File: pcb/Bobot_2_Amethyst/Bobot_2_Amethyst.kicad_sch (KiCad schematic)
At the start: 2 parts

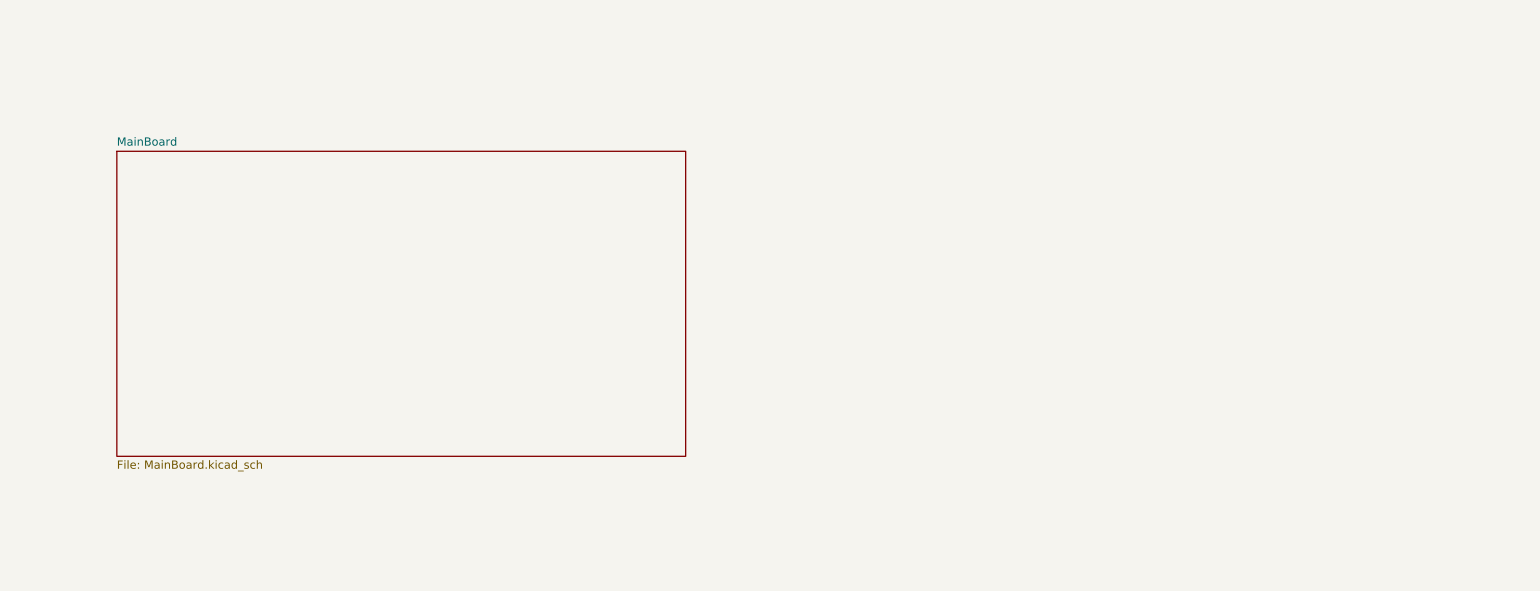
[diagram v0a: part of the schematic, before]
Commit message: pcb: add touch sensor board
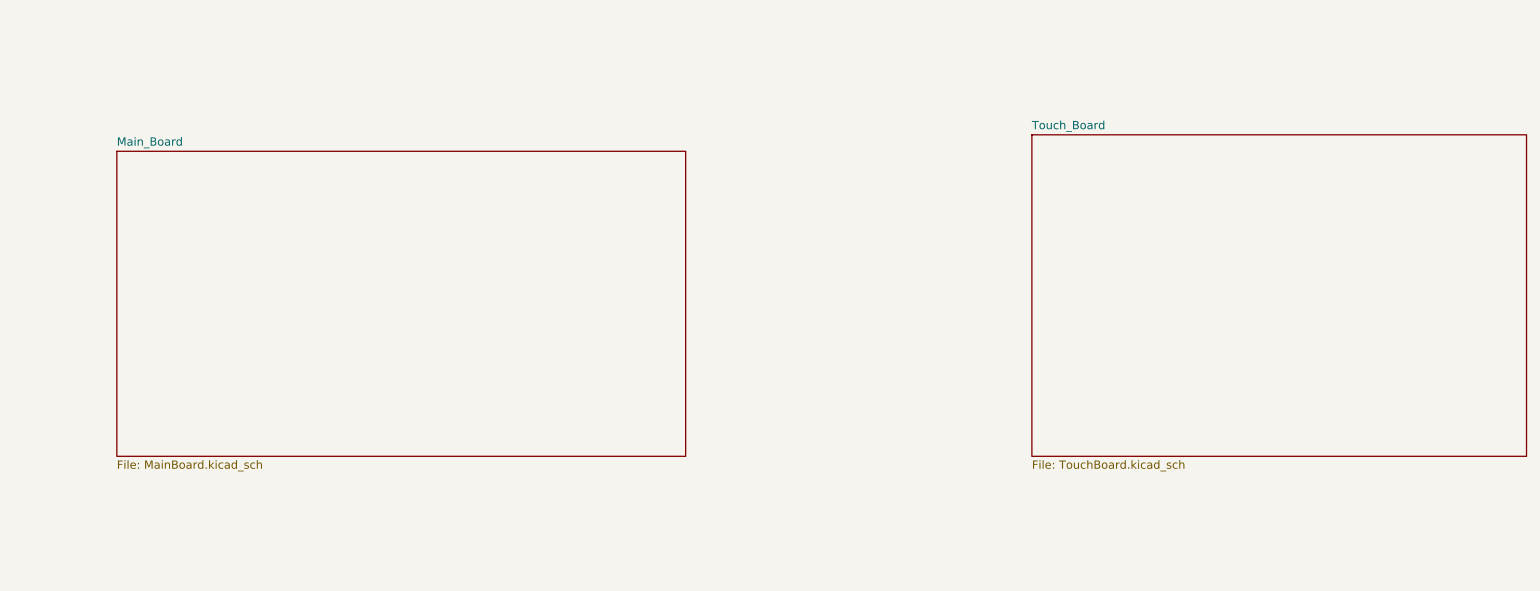
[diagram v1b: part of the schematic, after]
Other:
- sheet MainBoard renamed Main_Board
- added sheet Touch_Board (TouchBoard.kicad_sch)
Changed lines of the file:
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@@
 			(color 0 0 0 0.0000)
 		)
-		(property "Sheetname" "MainBoard"
+		(property "Sheetname" "Main_Board"
 			(at 204.47 84.3784 0)
 			(show_name yes)
@@
 				)
 			)
+		)
+	)
+	(sheet
+		(at 345.44 82.55)
+		(size 76.2 49.53)
+		(exclude_from_sim no)
+		(in_bom yes)
+		(on_board yes)
+		(dnp no)
+		(fields_autoplaced yes)
+		(stroke
+			(width 0.1524)
+			(type solid)
+		)
+		(fill
+			(color 0 0 0 0.0000)
+		)
+		(property "Sheetname" "Touch_Board"
+			(at 345.44 81.8384 0)
+			(effects
+				(font
+					(size 1.27 1.27)
+				)
+				(justify left bottom)
+			)
+		)
+		(property "Sheetfile" "TouchBoard.kicad_sch"
+			(at 345.44 132.6646 0)
+			(effects
+				(font
+					(size 1.27 1.27)
+				)
+				(justify left top)
+			)
+		)
+		(instances
+			(project "Bobot_2_Amethyst"
+				(path "/bbdd708a-b2b6-43d3-a3a2-0b4b48b4101b"
+					(page "5")
+				)
+			)
